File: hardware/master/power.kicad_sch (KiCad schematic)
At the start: 37 parts, among them J901 POWER IN, J902 FRAME, SW901 GROUND LIFT, U901 LM317, U902 LM337, U903 L7805

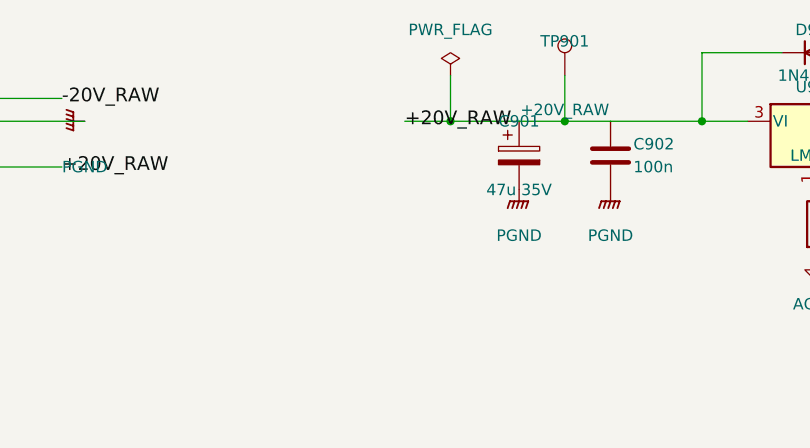
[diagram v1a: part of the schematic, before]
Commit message: Add master card master out sheet
SSI2162 master VCA with the channel fader law, soft clip in the I-V
stages, THAT1646 balanced drivers with offset caps and phantom clamps,
G6K output protection relays with 2 s power-up delay and raw-rail
drop-out (decision 92). Adds the THAT1646 symbol and exports
+20V_RAW from the power sheet.

Co-Authored-By: Claude Opus 5.5 <noreply@anthropic.com>
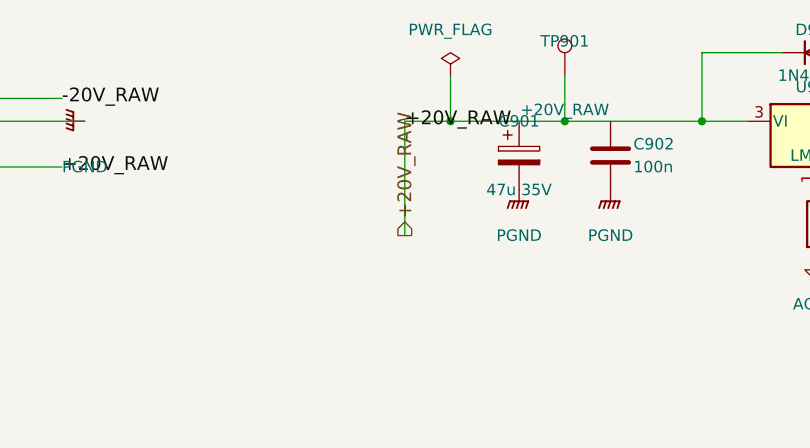
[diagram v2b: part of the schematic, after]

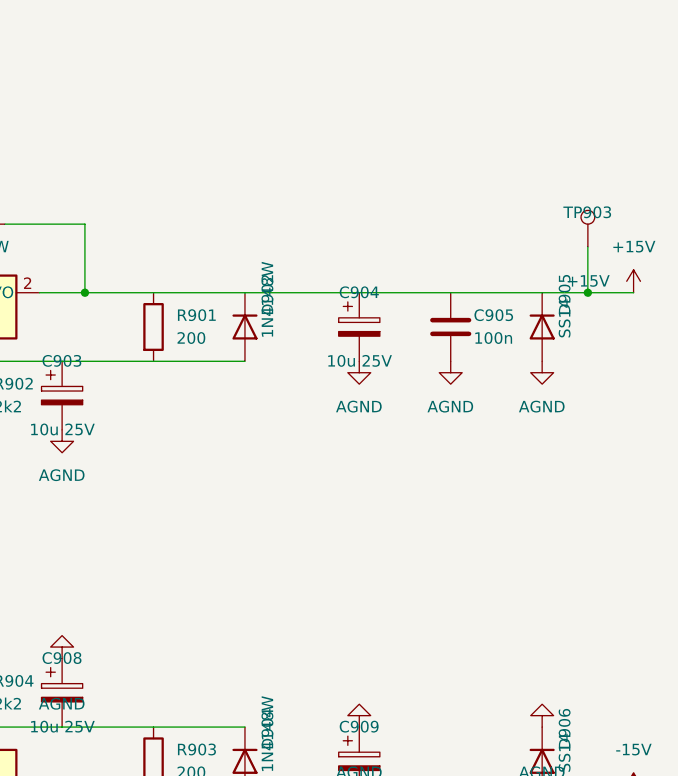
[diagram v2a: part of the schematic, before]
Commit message: Recheck master card power, add regulator heatsinks; update handoff
Power budget script for the master card (typical +15 V 345 mA,
-15 V 275 mA; worst case 730/606 mA) and board-mount TO-220 heatsinks
of 10 C/W or better on the LM317 and LM337 (decision 95). Handoff file
updated for the next session.

Co-Authored-By: Claude Opus 5.5 <noreply@anthropic.com>
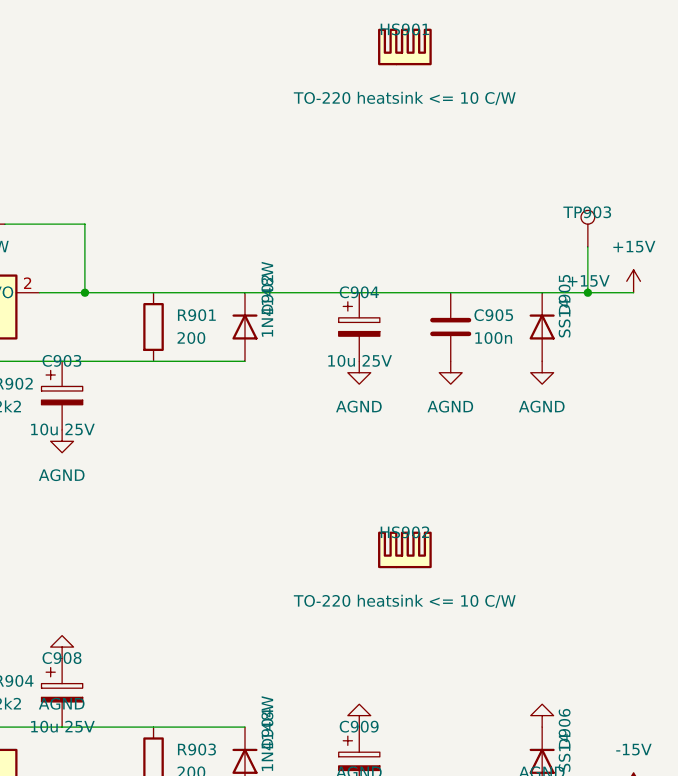
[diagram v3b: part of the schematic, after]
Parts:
- added HS901, HS902: TO-220 heatsink <= 10 C/W, symbol Mechanical:Heatsink

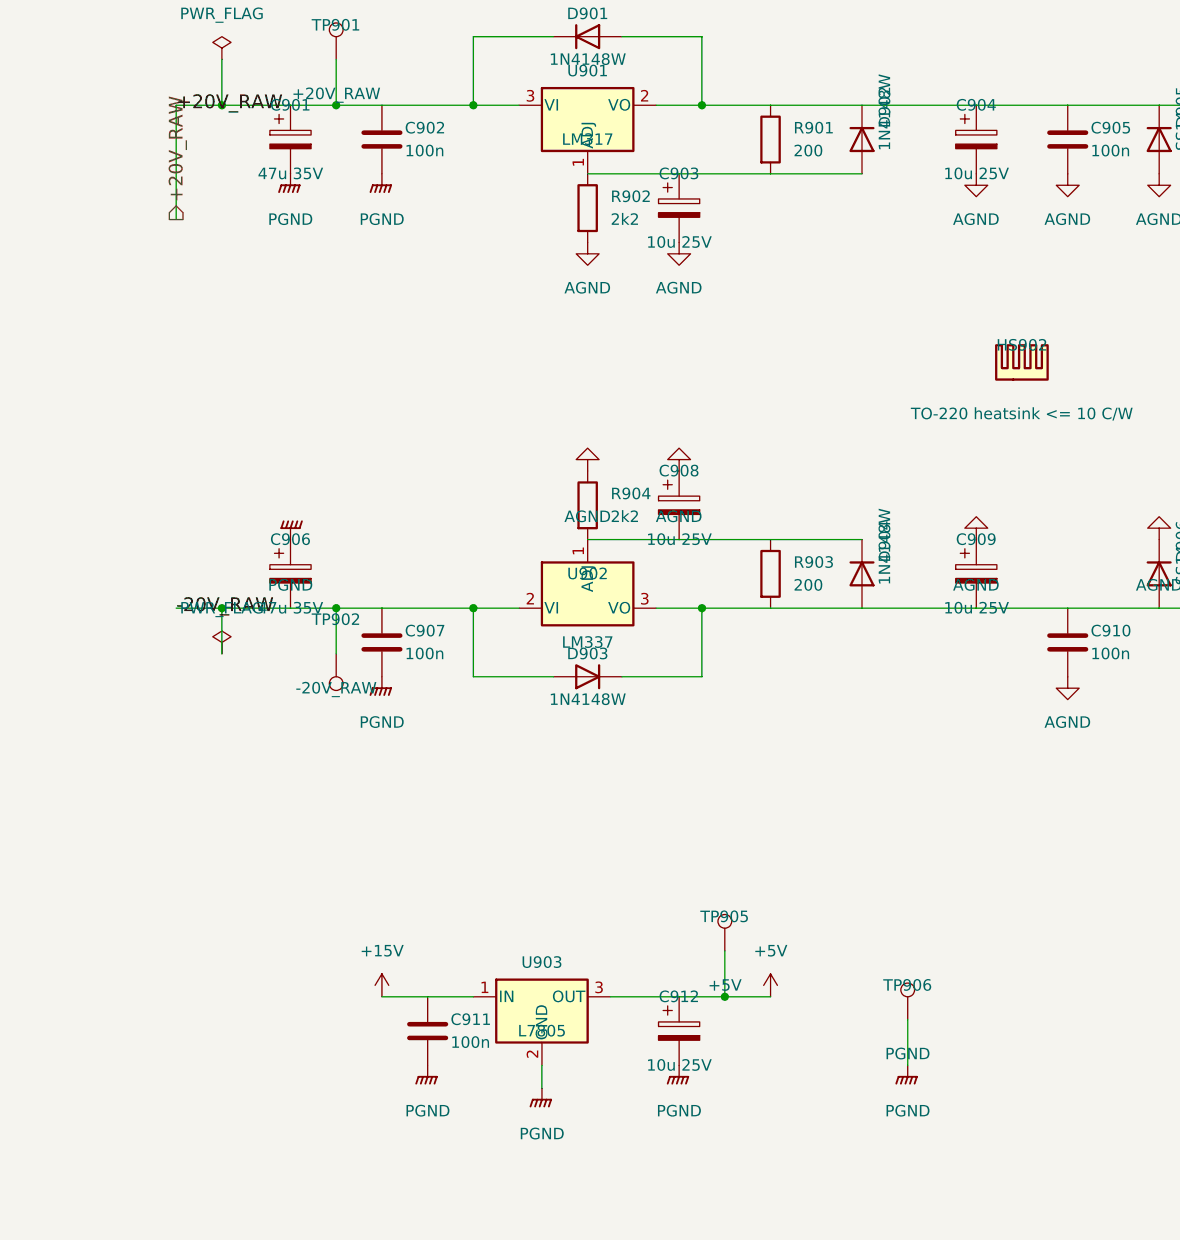
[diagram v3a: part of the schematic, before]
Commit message: Master card: DRV135 outputs, TL062 levers, SMD electrolytics, both raw rails watched (decisions 125-128)
/board master pre-layout session; the user delegated the open points.
- Confirms the [proposed] parts of decisions 89-94 (Q5 checked, +22 dB
  makeup kept for the breadboard, fallback R439 = 330k).
- 125: TI DRV135UA replaces the end-of-life THAT1646 (THAT memo
  2026-09-01); same SO-8 pinout, LCSC C544663.
- 126: U409, U410, U802, U804 TL072 -> TL062; superdiodes and U407 stay.
- 127: master electrolytics to SMD (decision 111 parts, 5.4 mm).
- 128: U707C watches -20V_RAW (22k6/100k), wired-OR with the +20 V trip.
- Würth fields on J101/J901, BAT54 LCSC C152458, G6K and header
  drawings checked, LCSC stock checked; budget 331/260 mA typical.
- parts.csv candidates for master pots and meter LEDs; lcsc_check.py
  handles MOhm.
ERC 0/0, all netlist checks 0 problems, reuse lint clean.

Co-Authored-By: Claude Opus 5.5 <noreply@anthropic.com>
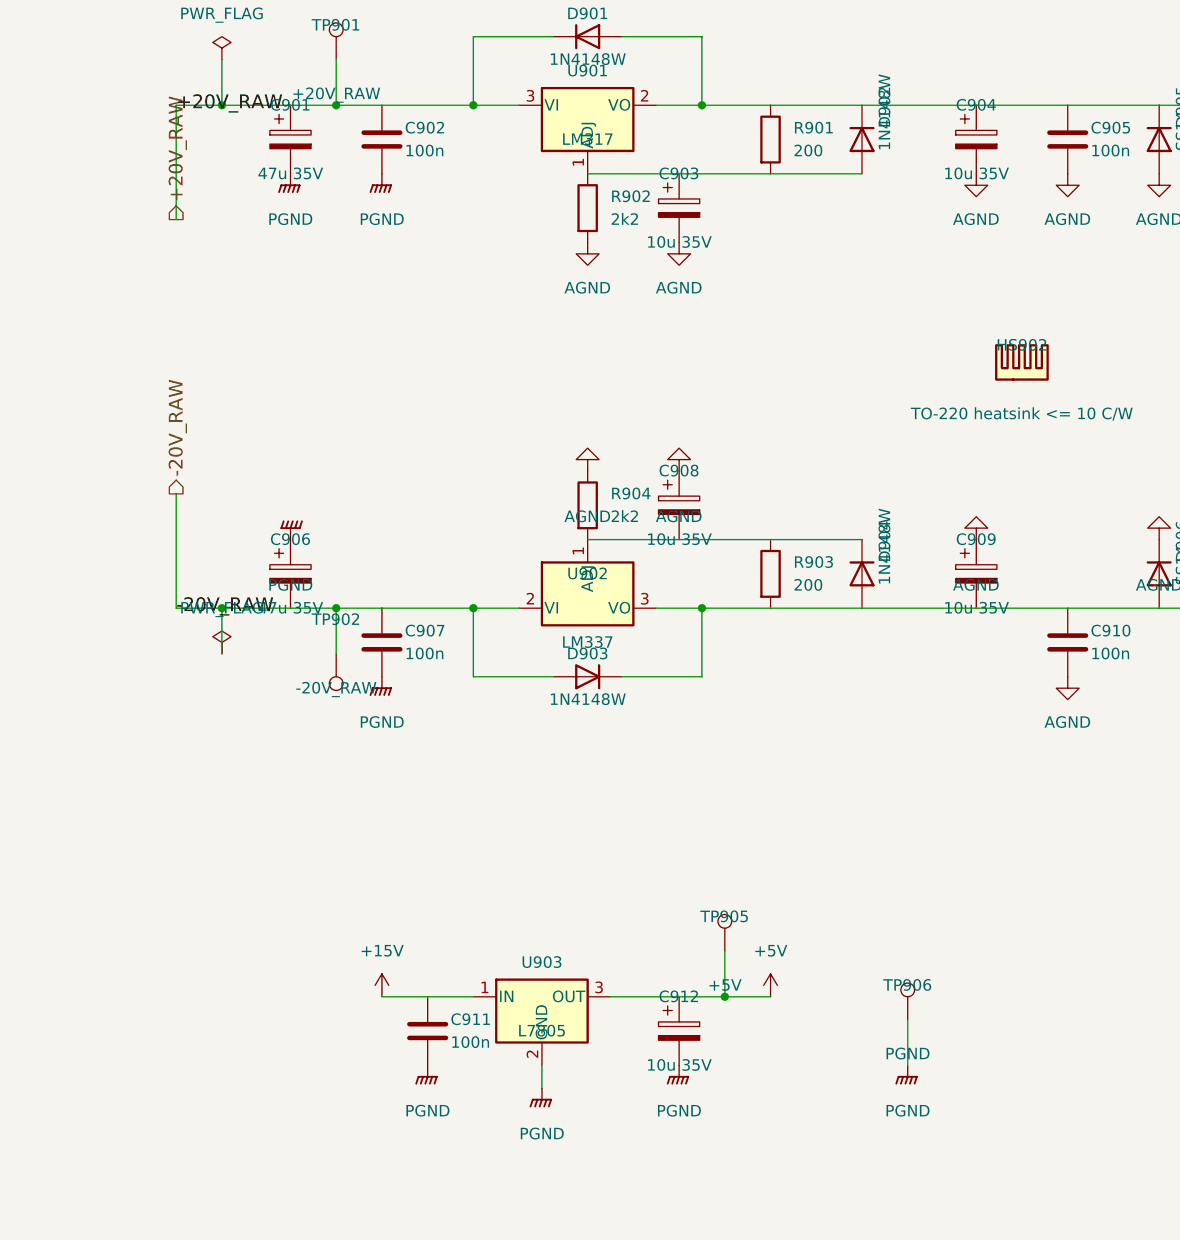
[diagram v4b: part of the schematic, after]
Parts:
- C901, C906: footprint Capacitor_THT:CP_Radial_D6.3mm_P2.50mm -> Capacitor_SMD:CP_Elec_6.3x5.4; MPN (none) -> RVT1V470M0605; Manufacturer (none) -> ROQANG; ProjectPN SX-C-011 -> SX-C-025; Supplier (none) -> LCSC; SupplierPN (none) -> C72522
- C903, C904, C908, C909, C912: value 10u 25V -> 10u 35V; footprint Capacitor_THT:CP_Radial_D5.0mm_P2.00mm -> Capacitor_SMD:CP_Elec_5x5.4; MPN (none) -> RVT1V100M0505; Manufacturer (none) -> ROQANG; ProjectPN SX-C-012 -> SX-C-024; Supplier (none) -> LCSC; SupplierPN (none) -> C72486
- J901: MPN (none) -> 61200821621; Manufacturer (none) -> Wurth Elektronik; Note 8-pin shrouded keyed box header: 1-2 V-, 3-6 PGND, 7-8 V+ (docs/CHAIN.md) -> 8-pin shrouded keyed box header: 1-2 V-, 3-6 PGND, 7-8 V+ (docs/CHAIN.md); drill 1.1 mm; Supplier (none) -> Mouser; SupplierPN (none) -> 710-61200821621

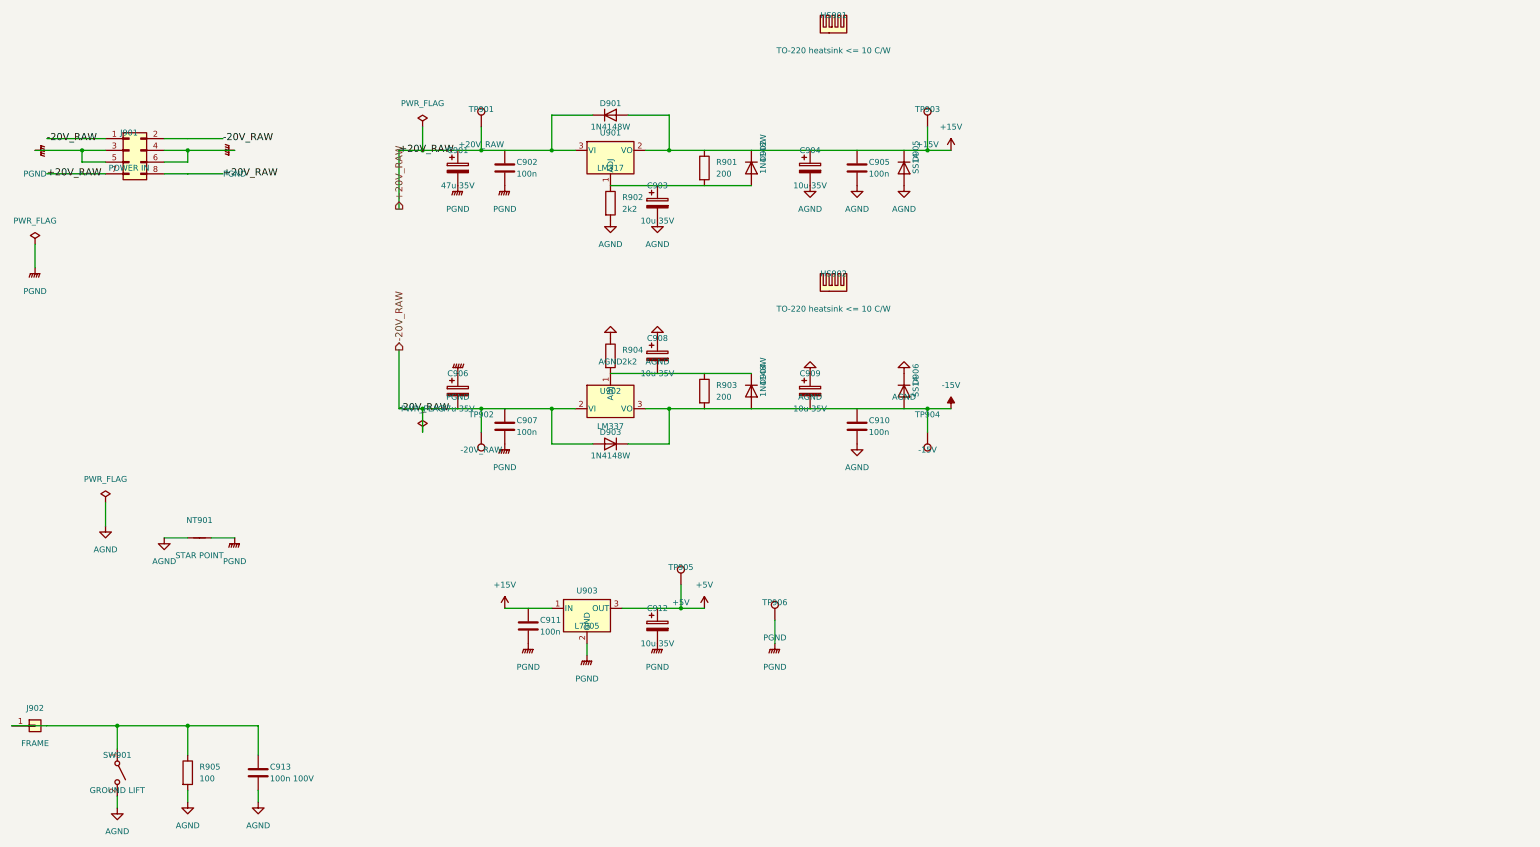
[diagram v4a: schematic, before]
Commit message: Master: rear jacks on two 26-pin row-board ribbons (decision 163)
J603 (AUX sends sheet) carries main outs and both AUX sends to the
output row board; J903 (Power sheet) brings the AUX returns, SC EXT
and the ground-lift switch (pins 25/26) from the input row board.
Pairs with a ground between them; row boards hold only jacks, header
and SW901. Netlist checks 0 problems, ERC 0/0.

Co-Authored-By: Claude Opus 5.5 <noreply@anthropic.com>
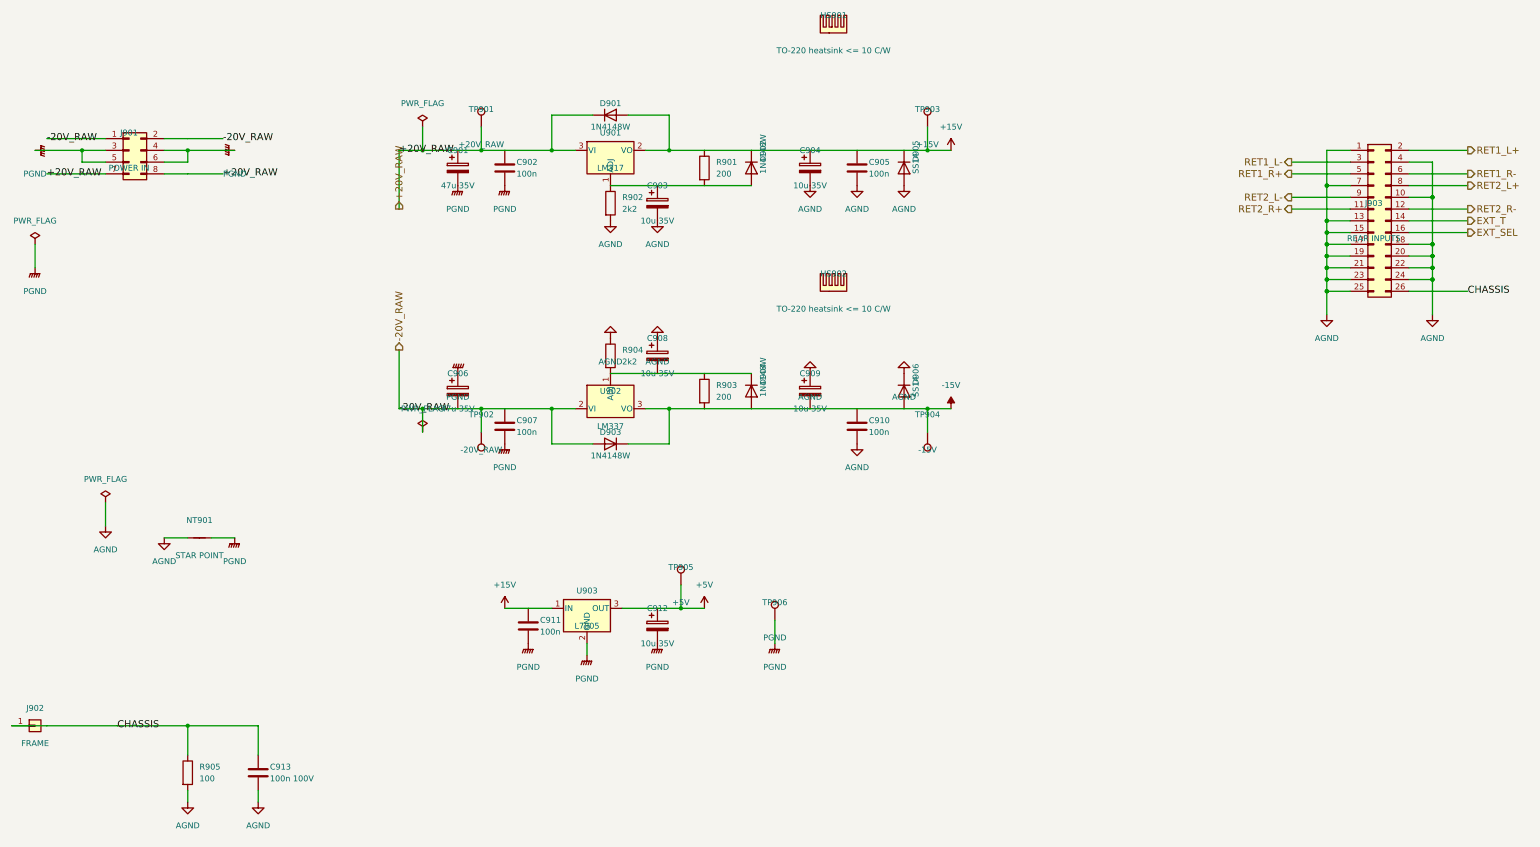
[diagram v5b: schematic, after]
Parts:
- removed SW901: GROUND LIFT, symbol Switch:SW_SPST
- added J903: REAR INPUTS, Connector_IDC:IDC-Header_2x13_P2.54mm_Vertical, symbol Connector_Generic:Conn_02x13_Odd_Even
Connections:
- net AGND: now also J903.1 (Pin_1), J903.10 (Pin_10), J903.13 (Pin_13), J903.15 (Pin_15), J903.17 (Pin_17), J903.18 (Pin_18), J903.19 (Pin_19), J903.20 (Pin_20), J903.21 (Pin_21), J903.22 (Pin_22), J903.23 (Pin_23), J903.24 (Pin_24), J903.25 (Pin_25), J903.4 (Pin_4), J903.7 (Pin_7)
- net CHASSIS: now reaches C913.1, J902.1 (Pin_1), R905.1
- net CHASSIS: now also J903.26 (Pin_26)
- new net EXT_SEL: J903.16 (Pin_16)
- new net EXT_T: J903.14 (Pin_14)
- new net RET1_L+: J903.2 (Pin_2)
- new net RET1_L-: J903.3 (Pin_3)
- new net RET1_R+: J903.5 (Pin_5)
- new net RET1_R-: J903.6 (Pin_6)
- new net RET2_L+: J903.8 (Pin_8)
- new net RET2_L-: J903.9 (Pin_9)
- new net RET2_R+: J903.11 (Pin_11)
- new net RET2_R-: J903.12 (Pin_12)

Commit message: Master: back-to-back coupling pairs, ten NE5532 to TL072, Wakefield heatsinks, onsemi TO-220 regulators (decisions 172-174)
Co-Authored-By: Claude Opus 5.5 <noreply@anthropic.com>
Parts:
- HS901, HS902: value TO-220 heatsink <= 10 C/W -> 637-10ABPE; MPN (none) -> 637-10ABPE; Manufacturer (none) -> Wakefield Thermal; Note Board-mount, live at the regulator tab: do not touch the ot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 -> Decision 174: vertical board mount on the underside, 25.4 m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; Supplier (none) -> Mouser; SupplierPN (none) -> 567-637-10ABPE
- U901: MPN LM317 -> LM317TG; Manufacturer Texas Instruments -> onsemi; Supplier (none) -> Mouser; SupplierPN (none) -> 863-LM317TG
- U902: MPN LM337 -> LM337TG; Manufacturer Texas Instruments -> onsemi; Supplier (none) -> Mouser; SupplierPN (none) -> 863-LM337TG
